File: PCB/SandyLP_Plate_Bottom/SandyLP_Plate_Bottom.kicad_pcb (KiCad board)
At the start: 2 copper layers, 285 x 94.6 mm, 32 parts

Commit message: ボトムプレート作成
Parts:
- removed the G*** at (208.0, 66.7)
- removed the G*** at (157.9, 64.0)
- removed H1, H2 (x7): MountingHole, MountingHole:MountingHole_2.2mm_M2
- removed the REF** at (157.9, 64.4)
- removed the REF** at (281.8, 26.3)
- removed the REF** at (72.2, 26.3)
- removed the REF** at (53.2, 26.3)
- removed the REF** at (148.4, 26.3)
- removed the REF** at (205.6, 26.3)
- removed the REF** at (91.3, 26.3)
- removed the REF** at (34.1, 26.3)
- removed the REF** at (24.6, 26.3)
- removed the REF** at (43.6, 83.5)
- removed the REF** at (262.7, 26.3)
- removed the REF** at (129.4, 26.3)
- removed the REF** at (272.2, 83.5)
- removed the REF** at (34.1, 45.4)
- removed the REF** at (167.5, 26.3)
- removed the REF** at (281.8, 45.4)
- removed the REF** at (243.7, 26.3)
- removed the REF** at (34.1, 64.4)
- removed the REF** at (281.8, 64.4)
- removed the REF** at (224.6, 26.3)
- removed the REF** at (186.5, 26.3)
- removed the REF** at (110.3, 26.3)
- added G***: LOGO, locallib:SandyLP_logo_w60, F.Cu at (158.0, 82.3)
- added G***: LOGO, locallib:SandyLP_QR_360dpi, B.Cu at (281.2, 50.1)
- added H_btm_1: MountingHole, locallib:MountingHole_2.2mm_M2_No_Cu, F.Cu at (23.9, 41.8)
- added H_btm_10: MountingHole, locallib:MountingHole_2.2mm_M2_No_Cu, F.Cu at (209.2, 112.1)
- added H_btm_11: MountingHole, locallib:MountingHole_2.2mm_M2_No_Cu, F.Cu at (293.6, 111.3)
- added H_btm_2: MountingHole, locallib:MountingHole_2.2mm_M2_No_Cu, F.Cu at (109.2, 37.7)
- added H_btm_3: MountingHole, locallib:MountingHole_2.2mm_M2_No_Cu, F.Cu at (209.2, 37.7)
- added H_btm_4: MountingHole, locallib:MountingHole_2.2mm_M2_No_Cu, F.Cu at (294.4, 41.8)
- added H_btm_5: MountingHole, locallib:MountingHole_2.2mm_M2_No_Cu, F.Cu at (63.9, 74.6)
- added H_btm_6: MountingHole, locallib:MountingHole_2.2mm_M2_No_Cu, F.Cu at (159.2, 74.6)
- added H_btm_7: MountingHole, locallib:MountingHole_2.2mm_M2_No_Cu, F.Cu at (254.4, 74.6)
- added H_btm_8: MountingHole, locallib:MountingHole_2.2mm_M2_No_Cu, F.Cu at (24.7, 111.3)
- added H_btm_9: MountingHole, locallib:MountingHole_2.2mm_M2_No_Cu, F.Cu at (106.8, 112.1)
- added LOGO1: Logo_Base, locallib:SandyLP_logo_w120, B.Cu at (164.5, 75.1)
- added REF**: 60_Outline, locallib:SandyLP_outline_Plate_Base_gentle_corner, F.Cu at (159.2, 84.2)
- added SW_/1: SW_Push, locallib:MXOnly-1U-Hotswap-guide-dummy, F.Cu at (273.5, 84.2)
- added SW_;1: SW_Push, locallib:MXOnly-1U-Hotswap-guide-dummy, F.Cu at (263.9, 65.1)
- added SW_<1: SW_Push, locallib:MXOnly-1U-Hotswap-guide-dummy, F.Cu at (235.4, 84.2)
- added SW_>1: SW_Push, locallib:MXOnly-1U-Hotswap-guide-dummy, F.Cu at (254.4, 84.2)
- added SW_A1: SW_Push, locallib:MXOnly-1U-Hotswap-guide-dummy, F.Cu at (54.4, 65.1)
- added SW_B1: SW_Push, locallib:MXOnly-1U-Hotswap-guide-dummy, F.Cu at (121.1, 84.2)
- added SW_C1: SW_Push, locallib:MXOnly-1U-Hotswap-guide-dummy, F.Cu at (83.0, 84.2)
- added SW_CTL1: SW_Push, locallib:MXOnly-1U-Hotswap-guide-dummy, F.Cu at (35.3, 65.1)
- added SW_D1: SW_Push, locallib:MXOnly-1U-Hotswap-guide-dummy, F.Cu at (92.5, 65.1)
- added SW_E1: SW_Push, locallib:MXOnly-1U-Hotswap-guide-dummy, F.Cu at (92.5, 46.1)
- added SW_ENT1: SW_Push, locallib:MXOnly-1U-Hotswap-guide-dummy, F.Cu at (283.0, 65.1)
- added SW_F1: SW_Push, locallib:MXOnly-1U-Hotswap-guide-dummy, F.Cu at (111.5, 65.1)
- added SW_I1: SW_Push, locallib:MXOnly-1U-Hotswap-guide-dummy, F.Cu at (225.8, 46.1)
- added SW_J1: SW_Push, locallib:MXOnly-1U-Hotswap-guide-dummy, F.Cu at (206.8, 65.1)
- added SW_K1: SW_Push, locallib:MXOnly-1U-Hotswap-guide-dummy, F.Cu at (225.8, 65.1)
- added SW_L1: SW_Push, locallib:MXOnly-1U-Hotswap-guide-dummy, F.Cu at (244.9, 65.1)
- added SW_LALTu1: SW_Push, locallib:MXOnly-1U-Hotswap-guide-dummy, F.Cu at (97.3, 103.2)
- added SW_LSPC1: SW_Push, locallib:MXOnly-1U-Hotswap-guide-dummy, F.Cu at (118.7, 103.2)
- added SW_LWIN1: SW_Push, locallib:MXOnly-1U-Hotswap-guide-dummy, F.Cu at (78.2, 103.2)
- added SW_M1: SW_Push, locallib:MXOnly-1U-Hotswap-guide-dummy, F.Cu at (216.3, 84.2)
- added SW_N1: SW_Push, locallib:MXOnly-1U-Hotswap-guide-dummy, F.Cu at (197.3, 84.2)
- added SW_O1: SW_Push, locallib:MXOnly-1U-Hotswap-guide-dummy, F.Cu at (244.9, 46.1)
- added SW_R5CNT_C1: RotaryEncoder_Switch, locallib:MXOnly-1U-Hotswap-guide-dummy, F.Cu at (159.2, 103.2)
- added SW_R5CNT_L1: SW_Push, locallib:MXOnly-1U-Hotswap-guide-dummy, F.Cu at (140.1, 103.2)
- added SW_R5CNT_R1: SW_Push, locallib:MXOnly-1U-Hotswap-guide-dummy, F.Cu at (178.2, 103.2)
- added SW_RALT1: SW_Push, locallib:MXOnly-1U-Hotswap-guide-dummy, F.Cu at (221.1, 103.2)
- added SW_RSPC1: SW_Push, locallib:MXOnly-1U-Hotswap-guide-dummy, F.Cu at (199.7, 103.2)
- added SW_RWIN1: SW_Push, locallib:MXOnly-1U-Hotswap-guide-dummy, F.Cu at (240.1, 103.2)
- added SW_S1: SW_Push, locallib:MXOnly-1U-Hotswap-guide-dummy, F.Cu at (73.4, 65.1)
- added SW_V1: SW_Push, locallib:MXOnly-1U-Hotswap-guide-dummy, F.Cu at (102.0, 84.2)
- added SW_W1: SW_Push, locallib:MXOnly-1U-Hotswap-guide-dummy, F.Cu at (73.4, 46.1)
- added SW_X1: SW_Push, locallib:MXOnly-1U-Hotswap-guide-dummy, F.Cu at (63.9, 84.2)
- added SW_Z1: SW_Push, locallib:MXOnly-1U-Hotswap-guide-dummy, F.Cu at (44.9, 84.2)
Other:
- board size 285 x 94.6 mm -> 275.5 x 80.3 mm
- board text added: "#SandyLP_kbd DN0010, Bottom by @jpskenn github.com/jpskenn/SandyLP"
- board text added: "Fairness, Justice, Rightness"
- board text removed: "JLCJLCJLCJLC"
- board text removed: "Sandy Bottom Plate by @jpskenn"
- board text removed: "USB connector"

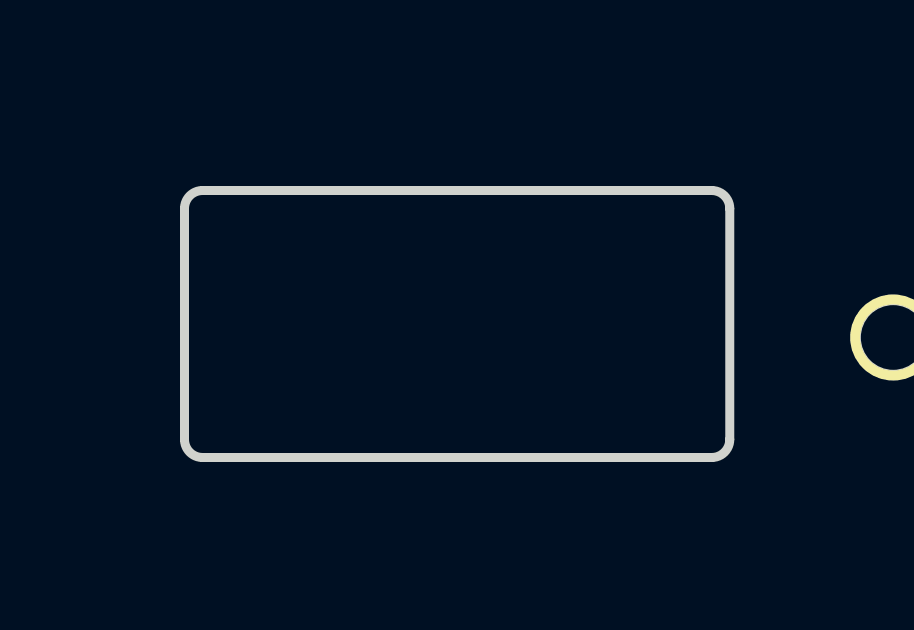
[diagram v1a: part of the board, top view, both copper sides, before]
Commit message: 底面ロゴのサイズを大きく
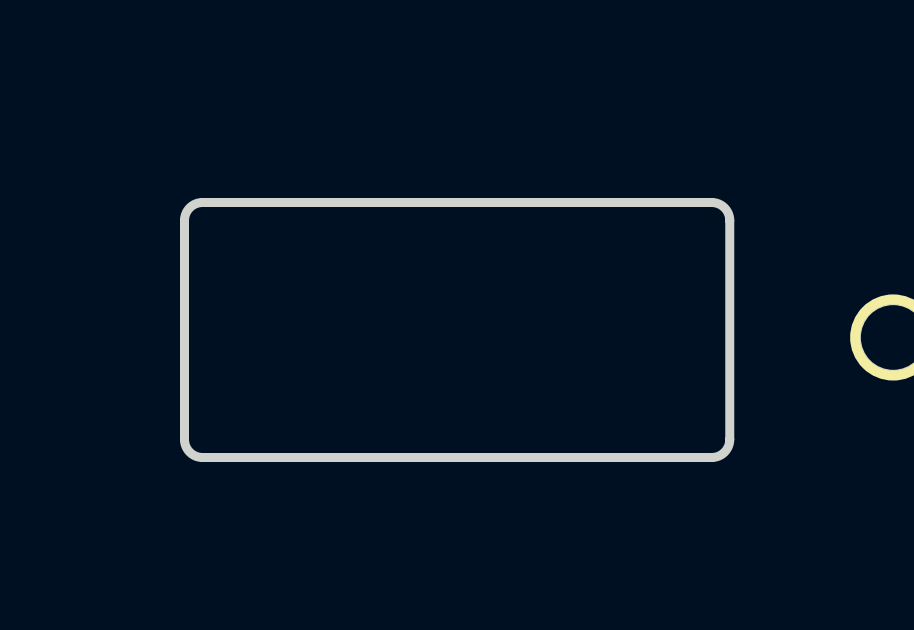
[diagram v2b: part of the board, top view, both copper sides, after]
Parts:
- removed LOGO1: Logo_Base, locallib:SandyLP_logo_w120
- added G***: LOGO, locallib:SandyLP_logo_h95, B.Cu at (165.1, 75.1)
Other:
- outline, holes or cut-outs redrawn

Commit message: ロゴを大きく
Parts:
- removed the G*** at (165.1, 75.1)
- added G***: LOGO, locallib:SandyLP_logo2_h115, B.Cu at (164.6, 82.5)

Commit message: QRコードの位置調整
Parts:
- removed the G*** at (281.2, 50.1)
- added G***: LOGO, locallib:SandyLP_QR_600dpi, B.Cu at (32.4, 109.1)

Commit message: ロゴ更新
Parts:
- removed the G*** at (158.0, 82.3)
- removed the G*** at (164.6, 82.5)
- added G***: LOGO, locallib:SandyLP_logo_LP40_h115, B.Cu at (170.2, 83.3)

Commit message: 基板Baseにスローガンを書いているので、こちらは削除。
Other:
- board text removed: "Fairness, Justice, Rightness"

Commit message: 基板Base左右角のネジ穴が近すぎるため、少し離した。
ナットとスペーサーを締める工具（十字レンチ）が入らないのを回避。
組み合わせるボトムプレートも、ネジ穴を同じ位置に変更。
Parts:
- moved H_btm_1 0.60 mm to (23.9, 42.4)
- moved H_btm_4 0.60 mm to (294.4, 42.4)
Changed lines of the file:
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@@
 		(allow_soldermask_bridges_in_footprints no)
 		(aux_axis_origin 16.295935 17.478405)
-		(grid_origin 21.049235 34.056081)
+		(grid_origin 16.295934 17.478405)
 		(pcbplotparams
 			(layerselection 0x00310fc_ffffffff)
@@
 		(locked yes)
 		(layer "F.Cu")
-		(at 23.895935 41.840905)
+		(at 23.895935 42.436218)
 		(descr "Mounting Hole 2.2mm, no annular, M2")
 		(tags "mounting hole 2.2mm no annular m2")
@@
 			(polygon
 				(pts
-					(xy 24.895935 39.640905) (xy 25.695935 40.240905) (xy 26.195935 41.040905) (xy 26.295935 41.840905)
-					(xy 26.195935 42.640905) (xy 25.695935 43.440905) (xy 24.895935 44.040905) (xy 23.895935 44.240905)
-					(xy 22.895935 44.040905) (xy 22.095935 43.440905) (xy 21.595935 42.640905) (xy 21.495935 41.840905)
-					(xy 21.595935 41.040905) (xy 22.095935 40.240905) (xy 22.895935 39.640905) (xy 23.895935 39.440905)
+					(xy 24.895935 40.236218) (xy 25.695935 40.836218) (xy 26.195935 41.636218) (xy 26.295935 42.436218)
+					(xy 26.195935 43.236218) (xy 25.695935 44.036218) (xy 24.895935 44.636218) (xy 23.895935 44.836218)
+					(xy 22.895935 44.636218) (xy 22.095935 44.036218) (xy 21.595935 43.236218) (xy 21.495935 42.436218)
+					(xy 21.595935 41.636218) (xy 22.095935 40.836218) (xy 22.895935 40.236218) (xy 23.895935 40.036218)
 				)
 			)
@@
 		(locked yes)
 		(layer "F.Cu")
-		(at 294.445935 41.840905)
+		(at 294.445935 42.436218)
 		(descr "Mounting Hole 2.2mm, no annular, M2")
 		(tags "mounting hole 2.2mm no annular m2")
@@
 			(polygon
 				(pts
-					(xy 295.445935 39.640905) (xy 296.245935 40.240905) (xy 296.745935 41.040905) (xy 296.845935 41.840905)
-					(xy 296.745935 42.640905) (xy 296.245935 43.440905) (xy 295.445935 44.040905) (xy 294.445935 44.240905)
-					(xy 293.445935 44.040905) (xy 292.645935 43.440905) (xy 292.145935 42.640905) (xy 292.045935 41.840905)
-					(xy 292.145935 41.040905) (xy 292.645935 40.240905) (xy 293.445935 39.640905) (xy 294.445935 39.440905)
+					(xy 295.445935 40.236218) (xy 296.245935 40.836218) (xy 296.745935 41.636218) (xy 296.845935 42.436218)
+					(xy 296.745935 43.236218) (xy 296.245935 44.036218) (xy 295.445935 44.636218) (xy 294.445935 44.836218)
+					(xy 293.445935 44.636218) (xy 292.645935 44.036218) (xy 292.145935 43.236218) (xy 292.045935 42.436218)
+					(xy 292.145935 41.636218) (xy 292.645935 40.836218) (xy 293.445935 40.236218) (xy 294.445935 40.036218)
 				)
 			)
